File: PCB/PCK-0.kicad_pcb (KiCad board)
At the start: 2 copper layers, 328.9 x 128.2 mm, 102 parts, among them J1 USB_C_Receptacle_USB2.0_16P, J2 BAT+, J3 BAT-, SW1 RotaryEncoder_Switch_MP, SW10 2,2, SW11 2,3, SW12 2,4, SW13 2,5, SW14 3,1, SW15 3,2, SW16 3,3, SW17 3,4, SW18 3,5, SW19 4,1, SW2 EN, SW20 4,2, SW21 4,3, SW22 4,4, SW23 4,5, SW24 5,1, SW25 5,2, SW26 5,3, SW27 5,4, SW28 5,5, SW29 6,1, SW3 BOOT, SW30 6,2, SW31 6,3, SW32 6,4, SW33 6,5, SW34 7,1, SW35 7,2, SW36 7,3, SW37 7,4, SW38 7,5, SW4 1,1, SW5 1,2, SW6 1,3, SW7 1,4, SW8 1,5, SW9 2,1, U1 NCP1117-3.3_SOT223, U2 TVS1400DRV, U3 NCP1117-3.3_SOT223, U4 USBLC6-2SC6, U5 ESP32-C6-MINI-1

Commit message: dont know lowkey
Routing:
- net /USB_D-: track 36.3 -> 39.8 mm
- net /USB_D+: track 37.5 -> 39.9 mm
- net Earth_Protective: vias 78 -> 0

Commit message: overhaul
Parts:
- removed D31, D32, D33, D34, D35, D36, D37: D, Diode_SMD:D_0805_2012Metric
- removed J2: BAT+, Connector_PinHeader_2.54mm:PinHeader_1x01_P2.54mm_Vertical
- removed J3: BAT-, Connector_PinHeader_2.54mm:PinHeader_1x01_P2.54mm_Vertical
- removed SW32: 6,4, Button_Switch_Keyboard:SW_Cherry_MX_1.00u_PCB
- removed SW33: 6,5, Button_Switch_Keyboard:SW_Cherry_MX_1.75u_PCB
- removed SW34: 7,1, Button_Switch_Keyboard:SW_Cherry_MX_1.00u_PCB
- removed SW35: 7,2, Button_Switch_Keyboard:SW_Cherry_MX_1.00u_PCB
- removed SW36: 7,3, Button_Switch_Keyboard:SW_Cherry_MX_1.00u_PCB
- removed SW37: 7,4, Button_Switch_Keyboard:SW_Cherry_MX_1.00u_PCB
- removed SW38: 7,5, Button_Switch_Keyboard:SW_Cherry_MX_1.00u_PCB
- BT1: footprint Battery:BatteryHolder_Keystone_1042_1x18650 -> Connector_PinHeader_2.54mm:PinHeader_1x02_P2.54mm_Horizontal
- C4: value 100n -> 10u
- C5: value 10u -> 100n
- D1: value BOOT_IND -> D
- D10, D11, D12, D13, D14, D15, D16, D17, D18, D19, D20, D21, D22, D23, D24, D25, D26, D27, D28, D3, D4, D5, D6, D7, D8, D9: moved to F.Cu
- D2: value BOOT_LIGHT -> D
- D29: value D -> BOOT_IND; moved to F.Cu
- D30: value D -> BOOT_LIGHT; moved to F.Cu
- R3, R4: value 470 -> 10k
- R6, R7: value 10k -> 470
- SW1: value RotaryEncoder_Switch_MP -> 1,1; footprint Rotary_Encoder:RotaryEncoder_Alps_EC12E-Switch_Vertical_H20mm_CircularMountingHoles -> Button_Switch_Keyboard:SW_Cherry_MX_1.50u_PCB
- SW10: value 2,2 -> 3,2
- SW11: value 2,3 -> 4,2
- SW12: value 2,4 -> 5,2
- SW13: value 2,5 -> 6,2
- SW14: value 3,1 -> 7,2
- SW15: value 3,2 -> EN; footprint Button_Switch_Keyboard:SW_Cherry_MX_1.00u_PCB -> Button_Switch_SMD:SW_Push_SPST_NO_Alps_SKRK
- SW16: value 3,3 -> 1,3; footprint Button_Switch_Keyboard:SW_Cherry_MX_1.00u_PCB -> Button_Switch_Keyboard:SW_Cherry_MX_1.50u_PCB
- SW17: value 3,4 -> 2,3
- SW18: value 3,5 -> 3,3
- SW19: value 4,1 -> 4,3
- SW2: value EN -> 2,1; footprint Button_Switch_SMD:SW_Push_SPST_NO_Alps_SKRK -> Button_Switch_Keyboard:SW_Cherry_MX_1.00u_PCB
- SW20: value 4,2 -> 5,3
- SW21: value 4,3 -> 6,3
- SW22: value 4,4 -> 7,3
- SW23: value 4,5 -> 1,4; footprint Button_Switch_Keyboard:SW_Cherry_MX_1.00u_PCB -> Button_Switch_Keyboard:SW_Cherry_MX_1.50u_PCB
- SW24: value 5,1 -> 2,4
- SW25: value 5,2 -> 3,4
- SW26: value 5,3 -> 4,4
- SW28: value 5,5 -> 6,4
- SW29: value 6,1 -> 7,4
- SW3: value BOOT -> 3,1; footprint Button_Switch_SMD:SW_Push_SPST_NO_Alps_SKRK -> Button_Switch_Keyboard:SW_Cherry_MX_1.00u_PCB
- SW30: value 6,2 -> BOOT; footprint Button_Switch_Keyboard:SW_Cherry_MX_1.00u_PCB -> Button_Switch_SMD:SW_Push_SPST_NO_Alps_SKRK
- SW31: value 6,3 -> RotaryEncoder_Switch_MP; footprint Button_Switch_Keyboard:SW_Cherry_MX_1.00u_PCB -> Rotary_Encoder:RotaryEncoder_Alps_EC12E-Switch_Vertical_H20mm_CircularMountingHoles
- SW4: value 1,1 -> 4,1; footprint Button_Switch_Keyboard:SW_Cherry_MX_1.50u_PCB -> Button_Switch_Keyboard:SW_Cherry_MX_1.00u_PCB
- SW5: value 1,2 -> 5,1; footprint Button_Switch_Keyboard:SW_Cherry_MX_1.50u_PCB -> Button_Switch_Keyboard:SW_Cherry_MX_1.00u_PCB
- SW6: value 1,3 -> 6,1; footprint Button_Switch_Keyboard:SW_Cherry_MX_1.50u_PCB -> Button_Switch_Keyboard:SW_Cherry_MX_1.00u_PCB
- SW7: value 1,4 -> 7,1; footprint Button_Switch_Keyboard:SW_Cherry_MX_1.50u_PCB -> Button_Switch_Keyboard:SW_Cherry_MX_1.00u_PCB
- SW8: value 1,5 -> 1,2
- SW9: value 2,1 -> 2,2
- U2: value TVS1400DRV -> NCP1117-3.3_SOT223; footprint Package_SON:WSON-6-1EP_2x2mm_P0.65mm_EP1x1.6mm -> Package_TO_SOT_SMD:SOT-223-3_TabPin2
- U3: value NCP1117-3.3_SOT223 -> USBLC6-2SC6; footprint Package_TO_SOT_SMD:SOT-223-3_TabPin2 -> Package_TO_SOT_SMD:SOT-23-6
- U4: value USBLC6-2SC6 -> ESP32-C6-MINI-1; footprint Package_TO_SOT_SMD:SOT-23-6 -> ESP32_C6_MINI_1U_H4:XCVR_ESP32-C6-MINI-1U-H4
- U5: value ESP32-C6-MINI-1 -> TVS1400DRV; footprint RF_Module:ESP32-C6-MINI-1 -> Package_SON:WSON-6-1EP_2x2mm_P0.65mm_EP1x1.6mm
- moved H3 419.7 mm to (73.7, 101.3)
- moved H1 419.6 mm to (73.7, 93.4)
- moved H4 419.6 mm to (73.7, 117.2)
- moved H2 419.5 mm to (73.7, 109.3)
- moved D2 275.5 mm to (66.6, 71.8), turned to 0 degrees
- moved D1 275.3 mm to (66.6, 59.7), turned to 0 degrees
- moved BT1 233.3 mm to (190.7, 43.8), turned to 180 degrees
- moved SW2 208.0 mm to (9.59, 85.0)
- moved SW3 191.6 mm to (24.7, 39.8)
- moved R4 186.2 mm to (154.8, 30.9), turned to 90 degrees
- moved R3 186.0 mm to (154.8, 34.3), turned to -90 degrees
- moved C5 173.4 mm to (147.1, 36.9)
- moved SW1 167.5 mm to (9.59, 24.7)
- moved U5 149.6 mm to (188.6, 40.6), turned to -90 degrees
- moved U3 147.7 mm to (171.8, 41.5), turned to 180 degrees
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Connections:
- BT1 pad 2: Earth_Protective -> GND
- C1 pad 2: Earth_Protective -> GND
- C2 pad 2: Earth_Protective -> GND
- C3 pad 2: Earth_Protective -> GND
- C4 pad 1: Earth_Protective -> +3V3
- C4 pad 2: VBUS -> GND
- C5 pad 1: +3V3 -> Net-(U4-EN)
- C5 pad 2: Earth_Protective -> GND
- C6 pad 1: Net-(U5-EN) -> GND
- C6 pad 2: Earth_Protective -> VBUS
- C7 pad 2: Earth_Protective -> GND
- D1 pad 1: /IO8 -> /IO19
- D10 pad 1: /IO21 -> /IO20
- D11 pad 1: /IO22 -> /IO20
- D12 pad 1: /IO23 -> /IO20
- D13 pad 1: /IO19 -> /IO20
- D16 pad 1: /IO22 -> /IO21
- D17 pad 1: /IO23 -> /IO21
- D18 pad 1: /IO19 -> /IO21
- D19 pad 1: /IO20 -> /IO21
- D2 pad 1: /IO9 -> /IO19
- D21 pad 1: /IO22 -> /IO21
- D22 pad 1: /IO23 -> /IO22
- D23 pad 1: /IO19 -> /IO22
- D24 pad 1: /IO20 -> /IO22
- D25 pad 1: /IO21 -> /IO22
- D27 pad 1: /IO23 -> /IO22
- D28 pad 1: /IO19 -> /IO22
- D29 pad 1: /IO20 -> /IO8
- D30 pad 1: /IO21 -> /IO9
- D4 pad 1: /IO20 -> /IO19
- D5 pad 1: /IO21 -> /IO19
- D6 pad 1: /IO22 -> /IO19
- D7 pad 1: /IO23 -> /IO19
- D8 pad 1: /IO19 -> /IO20
- H1 pad 1: Earth_Protective -> GND
- H2 pad 1: Earth_Protective -> GND
- H3 pad 1: Earth_Protective -> GND
- H4 pad 1: Earth_Protective -> GND
- J1 pad A1: Earth_Protective -> GND
- J1 pad A12: Earth_Protective -> GND
- J1 pad B1: Earth_Protective -> GND
- J1 pad B12: Earth_Protective -> GND
- J1 pad SH: Earth_Protective -> GND
- R1 pad 2: Earth_Protective -> GND
- R2 pad 2: Earth_Protective -> GND
- R3 pad 1: Net-(D1-A) -> +3V3
- R3 pad 2: +3V3 -> Net-(U4-EN)
- R4 pad 1: Net-(D2-A) -> +3V3
- R4 pad 2: +3V3 -> /IO9
- R5 pad 2: Net-(U5-EN) -> /IO8
- R6 pad 1: +3V3 -> Net-(D29-A)
- R6 pad 2: /IO9 -> +3V3
- R7 pad 1: +3V3 -> Net-(D30-A)
- R7 pad 2: /IO8 -> +3V3
- SW10 pad 1: /IO3 -> /IO4
- SW10 pad 2: Net-(D9-A) -> Net-(D10-A)
- SW11 pad 1: /IO3 -> /IO5
- SW11 pad 2: Net-(D10-A) -> Net-(D11-A)
- SW12 pad 1: /IO3 -> /IO0
- SW12 pad 2: Net-(D11-A) -> Net-(D12-A)
- SW13 pad 1: /IO3 -> /IO1
- SW13 pad 2: Net-(D12-A) -> Net-(D13-A)
- SW14 pad 1: /IO4 -> /IO6
- SW14 pad 2: Net-(D13-A) -> Net-(D14-A)
- SW15 pad 1: /IO4 -> GND
- SW15 pad 2: Net-(D14-A) -> Net-(U4-EN)
- SW16 pad 1: /IO4 -> /IO2
- SW17 pad 1: /IO4 -> /IO3
- SW2 pad 1: Earth_Protective -> /IO3
- SW2 pad 2: Net-(U5-EN) -> Net-(D2-A)
- SW20 pad 1: /IO5 -> /IO0
- SW21 pad 1: /IO5 -> /IO1
- SW22 pad 1: /IO5 -> /IO6
- SW23 pad 1: /IO5 -> /IO2
- SW24 pad 1: /IO0 -> /IO3
- SW25 pad 1: /IO0 -> /IO4
- SW26 pad 1: /IO0 -> /IO5
- SW28 pad 1: /IO0 -> /IO1
- SW29 pad 1: /IO1 -> /IO6
- SW3 pad 1: Earth_Protective -> /IO4
- SW3 pad 2: /IO9 -> Net-(D3-A)
- SW30 pad 1: /IO1 -> GND
- SW30 pad 2: Net-(D29-A) -> /IO9
- SW4 pad 1: /IO2 -> /IO5
- SW4 pad 2: Net-(D3-A) -> Net-(D4-A)
- SW5 pad 1: /IO2 -> /IO0
- SW5 pad 2: Net-(D4-A) -> Net-(D5-A)
- SW6 pad 1: /IO2 -> /IO1
- SW6 pad 2: Net-(D5-A) -> Net-(D6-A)
- SW7 pad 1: /IO2 -> /IO6
- SW7 pad 2: Net-(D6-A) -> Net-(D7-A)
- SW8 pad 2: Net-(D7-A) -> Net-(D8-A)
- SW9 pad 2: Net-(D8-A) -> Net-(D9-A)
- U1 pad 1: Earth_Protective -> GND
- U2 pad 1: Earth_Protective -> GND
- U2 pad 2: Earth_Protective -> +3V3
- U2 pad 3: Earth_Protective -> VBAT
- U3 pad 1: Earth_Protective -> /D-
- U3 pad 2: +3V3 -> GND
- U3 pad 3: VBAT -> /D+
- U4 pad 1: /D- -> GND
- U4 pad 2: Earth_Protective -> GND
- U4 pad 3: /D+ -> +3V3
- U4 pad 4: /USB_D+ -> unconnected-(U4-NC-Pad4)
- U4 pad 5: VBUS -> /IO2
- U4 pad 6: /USB_D- -> /IO3
- U5 pad 1: Earth_Protective -> GND
- U5 pad 2: Earth_Protective -> GND
- U5 pad 3: +3V3 -> GND
- U5 pad 4: unconnected-(U5-NC-Pad4) -> VBAT
- U5 pad 5: /IO2 -> VBAT
- U5 pad 6: /IO3 -> VBAT
- U5 pad 7: unconnected-(U5-NC-Pad7) -> GND
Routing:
- net /IO22: track 119.6 -> 15.1 mm, vias 0 -> 2
- net /IO23: track 114.6 -> 15.1 mm, vias 0 -> 2
- net /IO6: track 106.9 -> 7.43 mm, vias 0 -> 2
- net /IO19: track 98.8 -> 0.00 mm
- net /IO20: track 98.8 -> 16.4 mm, vias 0 -> 2
- net /IO21: track 98.8 -> 16.8 mm, vias 0 -> 2
- net /IO1: track 81.8 -> 5.20 mm, vias 1 -> 2
- net /IO5: track 77.3 -> 1.20 mm
- net /IO4: track 77.3 -> 1.20 mm
- net /IO0: track 78.5 -> 4.04 mm, vias 1 -> 2
- net /IO3: track 77.3 -> 6.68 mm, vias 1 -> 2
- net /IO2: track 77.3 -> 8.97 mm, vias 1 -> 2
- net +3V3: track 14.6 -> 60.3 mm, vias 0 -> 19
- net /USB_D+: track 39.9 -> 9.93 mm
- net /USB_D-: track 39.8 -> 10.7 mm
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- added copper zone on In2.Cu, net +3V3
- added copper zone on F.Cu, net GND
- added copper zone on In1.Cu, net GND
- removed copper zone on F.Cu, net Earth_Protective
- removed copper zone on F.Cu, net VBUS
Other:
- board size 328.9 x 128.2 mm -> 59.9 x 23.4 mm
- copper layers 2 -> 4

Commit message: one must imagine sisyphus happy
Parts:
- moved H1 157.3 mm to (230.0, 111.2)
- moved H2 157.3 mm to (230.0, 127.0)
- moved H3 157.3 mm to (230.0, 119.1)
- moved H4 157.3 mm to (230.0, 135.0)
- moved SW26 91.9 mm to (30.7, 116.4)
- moved SW9 87.4 mm to (106.9, 59.2)
- moved C4 83.2 mm to (151.4, 104.7), turned to 0 degrees
- moved D25 82.1 mm to (35.4, 130.7), turned to 135 degrees
- moved SW28 81.9 mm to (68.8, 116.4)
- moved C2 81.4 mm to (146.5, 104.7), turned to 0 degrees
- moved SW30 80.5 mm to (106.9, 116.4)
- moved D29 80.5 mm to (111.6, 130.7), turned to 135 degrees
- moved SW3 80.4 mm to (137.5, 120.8)
- moved D30 80.0 mm to (130.7, 130.7), turned to 135 degrees
- moved BT1 79.9 mm to (139.1, 104.7), turned to 90 degrees
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- renumbered D29 to D1, D8 to D10, D9 to D11, D10 to D12, D11 to D13, D12 to D14, D13 to D15, D14 to D16, D15 to D17, D16 to D18, D17 to D19, D30 to D2, D18 to D20, D19 to D21, D20 to D22, D21 to D23, D22 to D24, D23 to D25, D24 to D26, D25 to D27, D26 to D28, D27 to D29, D1 to D3, D28 to D30, D2 to D4, D3 to D5, D4 to D6, D5 to D7, D6 to D8, D7 to D9, SW15 to SW1, SW7 to SW10, SW8 to SW11, SW9 to SW12, SW10 to SW13, SW11 to SW14, SW12 to SW15, SW13 to SW16, SW14 to SW17, SW16 to SW18, SW17 to SW19, SW30 to SW2, SW18 to SW20, SW19 to SW21, SW20 to SW22, SW21 to SW23, SW22 to SW24, SW23 to SW25, SW24 to SW26, SW25 to SW27, SW26 to SW28, SW27 to SW29, SW31 to SW3, SW28 to SW30, SW29 to SW31, SW1 to SW4, SW2 to SW5, SW3 to SW6, SW4 to SW7, SW5 to SW8, SW6 to SW9
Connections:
- D10 pad 1: /IO20 -> /IO21
- D11 pad 1: /IO20 -> /IO21
- D12 pad 1: /IO20 -> /IO21
- D13 pad 1: /IO20 -> /IO21
- D14 pad 1: /IO20 -> /IO21
- D15 pad 1: /IO20 -> /IO21
- D16 pad 1: /IO20 -> /IO21
- D17 pad 1: /IO21 -> /IO6
- D18 pad 1: /IO21 -> /IO6
- D19 pad 1: /IO21 -> /IO6
- D20 pad 1: /IO21 -> /IO6
- D21 pad 1: /IO21 -> /IO6
- D22 pad 1: /IO21 -> /IO6
- D23 pad 1: /IO21 -> /IO6
- D24 pad 1: /IO22 -> /IO7
- D25 pad 1: /IO22 -> /IO7
- D26 pad 1: /IO22 -> /IO7
- D27 pad 1: /IO22 -> /IO7
- D28 pad 1: /IO22 -> /IO7
- D29 pad 1: /IO22 -> /IO7
- D3 pad 1: /IO19 -> /IO1
- D30 pad 1: /IO22 -> /IO7
- D4 pad 1: /IO19 -> /IO1
- D5 pad 1: /IO19 -> /IO1
- D6 pad 1: /IO19 -> /IO1
- D7 pad 1: /IO19 -> /IO1
- D8 pad 1: /IO19 -> /IO1
- D9 pad 1: /IO19 -> /IO1
- SW10 pad 1: /IO6 -> /IO0
- SW11 pad 1: /IO2 -> /IO4
- SW12 pad 1: /IO3 -> /IO5
- SW13 pad 1: /IO4 -> /IO3
- SW14 pad 1: /IO5 -> /IO2
- SW15 pad 1: /IO0 -> /IO23
- SW16 pad 1: /IO1 -> /IO22
- SW17 pad 1: /IO6 -> /IO0
- SW18 pad 1: /IO2 -> /IO4
- SW19 pad 1: /IO3 -> /IO5
- SW20 pad 1: /IO4 -> /IO3
- SW21 pad 1: /IO5 -> /IO2
- SW22 pad 1: /IO0 -> /IO23
- SW23 pad 1: /IO1 -> /IO22
- SW24 pad 1: /IO6 -> /IO0
- SW25 pad 1: /IO2 -> /IO4
- SW26 pad 1: /IO3 -> /IO5
- SW27 pad 1: /IO4 -> /IO3
- SW28 pad 1: /IO5 -> /IO2
- SW29 pad 1: /IO0 -> /IO23
- SW30 pad 1: /IO1 -> /IO22
- SW31 pad 1: /IO6 -> /IO0
- SW4 pad 1: /IO2 -> /IO4
- SW5 pad 1: /IO3 -> /IO5
- SW6 pad 1: /IO4 -> /IO3
- SW7 pad 1: /IO5 -> /IO2
- SW8 pad 1: /IO0 -> /IO23
- SW9 pad 1: /IO1 -> /IO22
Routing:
- net /IO4: track 1.20 -> 11.3 mm
- net /IO18: track 17.5 -> 7.87 mm
- net /IO5: track 1.20 -> 10.2 mm
- net /IO3: track 6.68 -> 13.5 mm
- net /IO15: track 13.7 -> 6.88 mm
- net /IO2: track 8.97 -> 14.7 mm
- net /IO14: track 11.6 -> 6.88 mm
- net /IO23: track 15.1 -> 19.8 mm
- net /IO22: track 15.1 -> 18.7 mm
- net /IO20: track 16.4 -> 13.2 mm
- net /IO0: track 4.04 -> 6.55 mm
- net /IO7: track 8.59 -> 6.55 mm
- net /IO1: track 5.20 -> 6.55 mm
- net /IO6: track 7.43 -> 6.55 mm
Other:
- board size 59.9 x 23.4 mm -> 166.7 x 78 mm

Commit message: reformat + modular control scheme
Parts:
- removed the D16 at (130.7, 92.6)
- removed the D23 at (130.7, 111.6)
- removed the D9 at (130.7, 73.5)
- removed the SW10 at (125.9, 59.2)
- removed the SW17 at (125.9, 78.3)
- removed the SW24 at (125.9, 97.3)
- added D27: D, Diode_SMD:D_0805_2012Metric, B.Cu at (74.2, 104.5)
- added D28: D, Diode_SMD:D_0805_2012Metric, B.Cu at (97.2, 107.3)
- added D29: D, Diode_SMD:D_0805_2012Metric, B.Cu at (116.7, 106.5)
- added D31: D, Diode_SMD:D_0805_2012Metric, B.Cu at (139.1, 76.0)
- added D32: D, Diode_SMD:D_0805_2012Metric, B.Cu at (139.1, 56.9)
- added J4: Conn_01x15, Connector_PinHeader_1.00mm:PinHeader_1x15_P1.00mm_Horizontal, F.Cu at (189.1, 59.6)
- added SW28: 1,4, kb_switch:Kailh_socket_MX_reversible, F.Cu at (84.2, 113.3)
- added SW29: 2,4, kb_switch:Kailh_socket_MX_reversible, F.Cu at (106.2, 114.3)
- added SW30: 3,4, kb_switch:Kailh_socket_MX_reversible, F.Cu at (128.2, 117.3)
- added SW32: 5,4, kb_switch:Kailh_socket_MX_reversible, F.Cu at (147.6, 66.7)
- added SW33: 6,4, kb_switch:Kailh_socket_MX_reversible, F.Cu at (147.6, 47.6)
- C1, C2, C3, C4, C5, C6, C7: footprint Diode_SMD:D_0805_2012Metric -> Capacitor_SMD:C_0805_2012Metric
- D10: renamed from D11; moved to B.Cu
- D11: renamed from D12; moved to B.Cu
- D12: renamed from D13; moved to B.Cu
- D13: renamed from D14; moved to B.Cu
- D14: renamed from D15; moved to B.Cu
- D15: renamed from D17; moved to B.Cu
- D16: renamed from D18; moved to B.Cu
- D17: renamed from D19; moved to B.Cu
- D18: renamed from D20; moved to B.Cu
- D19: renamed from D21; moved to B.Cu
- D20: renamed from D22; moved to B.Cu
- D21: renamed from D24; moved to B.Cu
- D22: renamed from D25; moved to B.Cu
- D23: renamed from D26; moved to B.Cu
- D24: renamed from D27; moved to B.Cu
- D25: renamed from D28; moved to B.Cu
- D26: renamed from D29; moved to B.Cu
- D3, D30, D4, D5, D6, D7, D8: moved to B.Cu
- D9: renamed from D10; moved to B.Cu
- R1, R2, R3, R4, R5, R6, R7: footprint Capacitor_SMD:C_0603_1608Metric -> Resistor_SMD:R_0603_1608Metric
- SW10: renamed from SW11; footprint Button_Switch_Keyboard:SW_Cherry_MX_1.50u_PCB -> kb_switch:Kailh_socket_MX_reversible
- SW11: renamed from SW12; footprint Button_Switch_Keyboard:SW_Cherry_MX_1.00u_PCB -> kb_switch:Kailh_socket_MX_reversible
- SW12: renamed from SW13; footprint Button_Switch_Keyboard:SW_Cherry_MX_1.00u_PCB -> kb_switch:Kailh_socket_MX_reversible
- SW13: renamed from SW14; footprint Button_Switch_Keyboard:SW_Cherry_MX_1.00u_PCB -> kb_switch:Kailh_socket_MX_reversible
- SW14: renamed from SW15; footprint Button_Switch_Keyboard:SW_Cherry_MX_1.00u_PCB -> kb_switch:Kailh_socket_MX_reversible
- SW15: renamed from SW16; footprint Button_Switch_Keyboard:SW_Cherry_MX_1.00u_PCB -> kb_switch:Kailh_socket_MX_reversible
- SW16: renamed from SW18; footprint Button_Switch_Keyboard:SW_Cherry_MX_1.50u_PCB -> kb_switch:Kailh_socket_MX_reversible
- SW17: renamed from SW19; footprint Button_Switch_Keyboard:SW_Cherry_MX_1.00u_PCB -> kb_switch:Kailh_socket_MX_reversible
- SW18: renamed from SW20; footprint Button_Switch_Keyboard:SW_Cherry_MX_1.00u_PCB -> kb_switch:Kailh_socket_MX_reversible
- SW19: renamed from SW21; footprint Button_Switch_Keyboard:SW_Cherry_MX_1.00u_PCB -> kb_switch:Kailh_socket_MX_reversible
- SW20: renamed from SW22; footprint Button_Switch_Keyboard:SW_Cherry_MX_1.00u_PCB -> kb_switch:Kailh_socket_MX_reversible
- SW21: renamed from SW23; footprint Button_Switch_Keyboard:SW_Cherry_MX_1.00u_PCB -> kb_switch:Kailh_socket_MX_reversible
- SW22: renamed from SW25; footprint Button_Switch_Keyboard:SW_Cherry_MX_1.50u_PCB -> kb_switch:Kailh_socket_MX_reversible
- SW23: renamed from SW26; footprint Button_Switch_Keyboard:SW_Cherry_MX_1.00u_PCB -> kb_switch:Kailh_socket_MX_reversible
- SW24: renamed from SW27; footprint Button_Switch_Keyboard:SW_Cherry_MX_1.00u_PCB -> kb_switch:Kailh_socket_MX_reversible
- SW25: renamed from SW28; footprint Button_Switch_Keyboard:SW_Cherry_MX_1.00u_PCB -> kb_switch:Kailh_socket_MX_reversible
- SW26: renamed from SW29; footprint Button_Switch_Keyboard:SW_Cherry_MX_1.00u_PCB -> kb_switch:Kailh_socket_MX_reversible
- SW27: renamed from SW30; footprint Button_Switch_Keyboard:SW_Cherry_MX_1.00u_PCB -> kb_switch:Kailh_socket_MX_reversible
- SW31: value 7,4 -> 4,4; footprint Button_Switch_Keyboard:SW_Cherry_MX_1.00u_PCB -> kb_switch:Kailh_socket_MX_reversible
- SW4: footprint Button_Switch_Keyboard:SW_Cherry_MX_1.50u_PCB -> kb_switch:Kailh_socket_MX_reversible
- SW5, SW6, SW7, SW8, SW9: footprint Button_Switch_Keyboard:SW_Cherry_MX_1.00u_PCB -> kb_switch:Kailh_socket_MX_reversible
- moved BT1 57.1 mm to (192.8, 85.5)
- moved U2 57.1 mm to (192.8, 77.4)
- moved C3 57.1 mm to (191.9, 83.2)
- moved U5 57.1 mm to (196.0, 83.4)
- moved C1 56.2 mm to (207.5, 80.7)
- moved C2 56.2 mm to (199.5, 85.9)
- moved C4 56.2 mm to (204.4, 85.9)
- moved C5 56.2 mm to (198.9, 42.3)
- moved C6 56.2 mm to (190.9, 67.0)
- moved C7 56.2 mm to (204.8, 42.3)
- moved D1 56.2 mm to (201.9, 43.0)
- moved D2 56.2 mm to (204.8, 44.5)
- moved J1 56.2 mm to (205.5, 71.1)
- moved R1 56.2 mm to (199.2, 73.1)
- moved R2 56.2 mm to (199.2, 68.5)
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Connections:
- D10 pad 1: /IO21 -> /IO1
- D11 pad 1: /IO21 -> /IO1
- D12 pad 1: /IO21 -> /IO1
- D13 pad 1: /IO21 -> /IO1
- D14 pad 1: /IO21 -> /IO1
- D15 pad 1: /IO6 -> /IO21
- D16 pad 1: /IO6 -> /IO21
- D17 pad 1: /IO6 -> /IO21
- D18 pad 1: /IO6 -> /IO21
- D19 pad 1: /IO6 -> /IO21
- D20 pad 1: /IO6 -> /IO21
- D21 pad 1: /IO7 -> /IO6
- D22 pad 1: /IO7 -> /IO6
- D23 pad 1: /IO7 -> /IO6
- D24 pad 1: /IO7 -> /IO6
- D25 pad 1: /IO7 -> /IO6
- D26 pad 1: /IO7 -> /IO6
- D3 pad 1: /IO1 -> /IO0
- D4 pad 1: /IO1 -> /IO0
- D5 pad 1: /IO1 -> /IO0
- D6 pad 1: /IO1 -> /IO0
- D7 pad 1: /IO1 -> /IO0
- D8 pad 1: /IO1 -> /IO0
- D9 pad 1: /IO21 -> /IO1
- SW3 pad A: /IO12 -> /IO20
- SW3 pad B: /IO14 -> /IO15
- SW3 pad C: /IO13 -> /IO14
- SW3 pad S1: /IO15 -> /IO18
- SW31 pad 1: /IO0 -> /IO2
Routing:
- net /IO23: track 19.8 -> 22.1 mm, vias 2 -> 1
- net /IO3: track 13.5 -> 15.7 mm
- net /IO4: track 11.3 -> 13.4 mm
- net /IO22: track 18.7 -> 20.8 mm, vias 2 -> 1
- net /IO5: track 10.2 -> 12.2 mm
- net /IO2: track 14.7 -> 16.6 mm
- net /IO0: track 6.55 -> 8.16 mm, vias 2 -> 1
- net /IO1: track 6.55 -> 8.08 mm, vias 2 -> 1
- net /IO21: track 16.9 -> 18.3 mm, vias 2 -> 1
- net /IO6: track 6.55 -> 7.91 mm, vias 2 -> 1
- net /IO7: track 6.55 -> 7.83 mm, vias 2 -> 1
- net /IO20: track 13.2 -> 14.4 mm, vias 2 -> 1
- net /IO14: track 6.88 -> 7.99 mm, vias 2 -> 1
- net /IO15: track 6.88 -> 7.91 mm, vias 2 -> 1
- net /IO18: track 7.87 -> 8.82 mm, vias 2 -> 1
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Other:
- board size 166.7 x 78 mm -> 187.6 x 103.5 mm

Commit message: double sided probably works
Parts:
- D10, D11, D12, D13, D14, D15, D16, D17, D18, D19, D20, D21, D22, D23, D24, D25, D26, D27, D28, D29, D3, D30, D31, D32, D4, D5, D6, D7, D8, D9: footprint Diode_SMD:D_0805_2012Metric -> Diode_THT:D_A-405_P2.54mm_Vertical_AnodeUp
- SW10, SW11, SW12, SW13, SW14, SW15, SW16, SW17, SW18, SW19, SW20, SW21, SW22, SW23, SW24, SW25, SW26, SW27, SW28, SW29, SW30, SW31, SW32, SW33, SW4, SW5, SW6, SW7, SW8, SW9: footprint kb_switch:Kailh_socket_MX_reversible -> KB_SWITCH:SW_MX_reversible
- moved C6 138.9 mm to (325.8, 33.5)
- moved D1 138.9 mm to (336.8, 9.59)
- moved R3 138.9 mm to (336.4, 16.5)
- moved U4 138.9 mm to (336.3, 24.6)
- moved C3 138.9 mm to (326.7, 49.8)
- moved C4 138.9 mm to (339.2, 52.4)
- moved C5 138.9 mm to (333.7, 8.85)
- moved C7 138.9 mm to (339.6, 8.85)
- moved D2 138.9 mm to (339.6, 11.0)
- moved J1 138.9 mm to (340.3, 37.6)
- moved R1 138.9 mm to (334.1, 39.6)
- moved R2 138.9 mm to (334.1, 35.1)
- moved R4 138.9 mm to (339.8, 16.5)
- moved R5 138.9 mm to (337.1, 13.8)
- moved R7 138.9 mm to (338.7, 13.8)
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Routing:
- net /IO3: vias 2 -> 1
- net /IO4: vias 1 -> 0
- net /IO5: vias 1 -> 0
- net /IO2: vias 2 -> 1
- net Net-(D9-A): vias 1 -> 0
- net Net-(D8-A): vias 1 -> 0
- net Net-(D7-A): vias 1 -> 0
- net Net-(D6-A): vias 1 -> 0
- net Net-(D5-A): vias 1 -> 0
- net Net-(D4-A): vias 1 -> 0
- net Net-(D32-A): vias 1 -> 0
- net Net-(D31-A): vias 1 -> 0
- net Net-(D30-A): vias 1 -> 0
- net Net-(D3-A): vias 1 -> 0
- net Net-(D29-A): vias 1 -> 0
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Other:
- board size 187.6 x 103.5 mm -> 321.9 x 127 mm

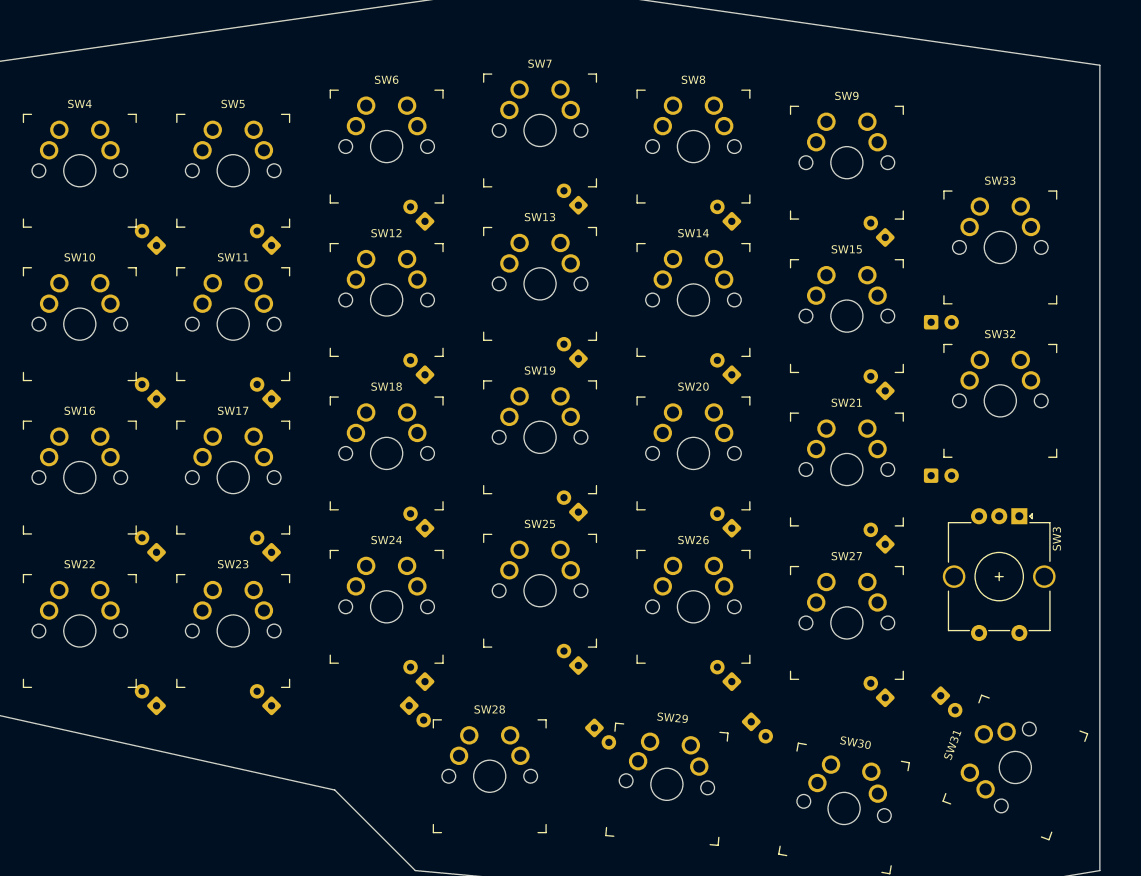
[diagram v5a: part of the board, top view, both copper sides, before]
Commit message: diode changed to SMD, mounting holes
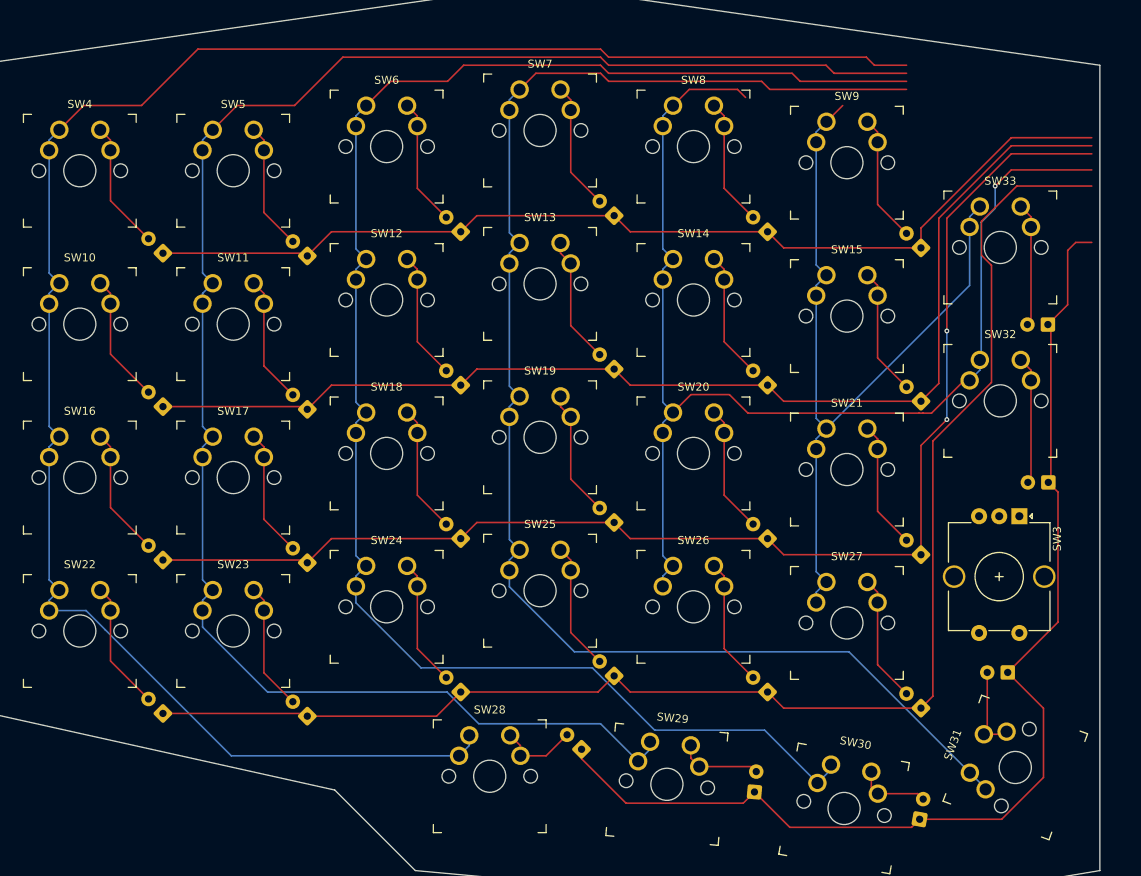
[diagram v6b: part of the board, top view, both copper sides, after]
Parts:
- moved D29 24.2 mm to (137.6, 118.6), turned to 80 degrees
- moved D27 22.1 mm to (95.6, 109.9), turned to 135 degrees
- moved D28 21.4 mm to (117.1, 115.2), turned to 85 degrees
- moved D31 14.6 mm to (153.6, 76.8), turned to 180 degrees
- moved D32 14.5 mm to (153.5, 57.2), turned to 180 degrees
- moved D30 8.80 mm to (148.6, 100.4), turned to 180 degrees
- moved D20 4.62 mm to (137.8, 85.8)
- moved D26 4.62 mm to (137.8, 104.8)
- moved D14 4.62 mm to (137.8, 66.7)
- moved D8 4.62 mm to (137.8, 47.7)
- moved D16 4.62 mm to (61.6, 86.8)
- moved D17 4.62 mm to (80.6, 83.8)
- moved D18 4.62 mm to (99.7, 81.8)
- moved D19 4.62 mm to (118.7, 83.8)
- moved D22 4.62 mm to (61.6, 105.8)
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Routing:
- net /IO4: track 13.4 -> 248.4 mm
- net /IO5: track 12.2 -> 232.3 mm
- net /IO3: track 15.7 -> 220.7 mm
- net /IO2: track 16.6 -> 201.3 mm
- net /IO6: track 7.91 -> 186.0 mm
- net /IO21: track 18.3 -> 180.7 mm, vias 1 -> 3
- net /IO23: track 22.1 -> 174.4 mm, vias 1 -> 2
- net /IO1: track 8.08 -> 152.4 mm
- net /IO7: track 7.83 -> 148.7 mm
- net /IO0: track 8.16 -> 134.5 mm
- net /IO22: track 20.8 -> 122.5 mm
- net Net-(D20-A): track 0.00 -> 17.1 mm
- net Net-(D9-A): track 0.00 -> 16.0 mm
- net Net-(D3-A): track 0.00 -> 16.0 mm
- net Net-(D21-A): track 0.00 -> 16.0 mm
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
